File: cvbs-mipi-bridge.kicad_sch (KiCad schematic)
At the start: 107 parts, among them IC1 ADV7280BCPZ-M, IC2 TLV70018, IC4 SN74AUP1G17DCKR, IC5 SN74AUP1G17DCKR, J1 WE_68715014522, J2 1053131102, J3 KLPX-0848A-2-Y, J4 KLPX-0848A-2-Y, J5 KLPX-0848A-2-Y, J6 KLPX-0848A-2-Y, J7 61300211121, Q1 BSS138APW, Q2 BSS138APW, Q3 BSS138APW, Q4 BSS138APW, Y1 ABM8G-28.63636MHZ-18-D2Y-T

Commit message: Routing (WiP)
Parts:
- removed R30: R_0R_0402, cvbs-mipi-bridge-footprints:0402-res, symbol cvbs-mipi-bridge:R_0R_0402
- added R30: R_0R_0805, cvbs-mipi-bridge-footprints:0805-res, symbol cvbs-mipi-bridge:R_0R_0805
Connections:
- net 1V8_SYS: now also R30.2
- net at C9.1, IC2.5 (VOUT), TP3.1: now also R30.1
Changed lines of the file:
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@@
     (pin "4")
-  )
-  (symbol (lib_id "cvbs-mipi-bridge:R_0R_0402") (at 174.625 36.83 0) (unit 1)
-    (in_bom yes) (on_board yes) (fields_autoplaced)
-    (property "Reference" "R30" (id 0) (at 174.625 31.8861 0)
-      (effects (font (size 1.524 1.524)))
-    )
-    (property "Value" "R_0R_0402" (id 1) (at 174.625 40.64 0)
-      (effects (font (size 1.524 1.524)) hide)
-    )
-    (property "Footprint" "cvbs-mipi-bridge-footprints:0402-res" (id 2) (at 179.705 31.75 0)
-      (effects (font (size 1.524 1.524)) (justify left) hide)
-    )
-    (property "Datasheet" "" (id 3) (at 174.625 36.83 0)
-      (effects (font (size 1.27 1.27)) hide)
-    )
-    (property "Manufacturer" "PANASONIC" (id 4) (at 179.705 26.67 0)
-      (effects (font (size 1.524 1.524)) (justify left) hide)
-    )
-    (property "MPN" "ERJ2GE0R00X" (id 5) (at 179.705 29.21 0)
-      (effects (font (size 1.524 1.524)) (justify left) hide)
-    )
-    (property "Val" "0R" (id 6) (at 174.625 34.6512 0))
-    (pin "1")
-    (pin "2")
   )
   (symbol (lib_id "cvbs-mipi-bridge:BSS138APW") (at 127 262.255 270) (unit 1)
@@
       (effects (font (size 1.524 1.524)) (justify left) hide)
     )
+    (pin "1")
+    (pin "2")
+  )
+  (symbol (lib_id "cvbs-mipi-bridge:R_0R_0805") (at 174.625 36.83 0) (unit 1)
+    (in_bom yes) (on_board yes)
+    (property "Reference" "R30" (id 0) (at 174.625 34.29 0)
+      (effects (font (size 1.524 1.524)))
+    )
+    (property "Value" "R_0R_0805" (id 1) (at 174.625 40.64 0)
+      (effects (font (size 1.524 1.524)) hide)
+    )
+    (property "Footprint" "cvbs-mipi-bridge-footprints:0805-res" (id 2) (at 179.705 31.75 0)
+      (effects (font (size 1.524 1.524)) (justify left) hide)
+    )
+    (property "Datasheet" "" (id 3) (at 174.625 36.83 0)
+      (effects (font (size 1.27 1.27)) hide)
+    )
+    (property "Manufacturer" "VISHAY" (id 4) (at 179.705 26.67 0)
+      (effects (font (size 1.524 1.524)) (justify left) hide)
+    )
+    (property "MPN" "CRCW08050000Z0EA" (id 5) (at 179.705 29.21 0)
+      (effects (font (size 1.524 1.524)) (justify left) hide)
+    )
+    (property "Val" "0R" (id 6) (at 174.625 39.37 0))
     (pin "1")
     (pin "2")
@@
       (reference "R29") (unit 1) (value "R_100k_0402") (footprint "cvbs-mipi-bridge-footprints:0402-res")
     )
-    (path "/935a0ed4-8ab8-4466-9793-5326c0b86bd1"
-      (reference "R30") (unit 1) (value "R_0R_0402") (footprint "cvbs-mipi-bridge-footprints:0402-res")
+    (path "/a2042ad6-c037-4bf6-86fd-f7cc9c142ea2"
+      (reference "R30") (unit 1) (value "R_0R_0805") (footprint "cvbs-mipi-bridge-footprints:0805-res")
     )
     (path "/61c0936f-710e-41ac-8508-01af59b77b09"

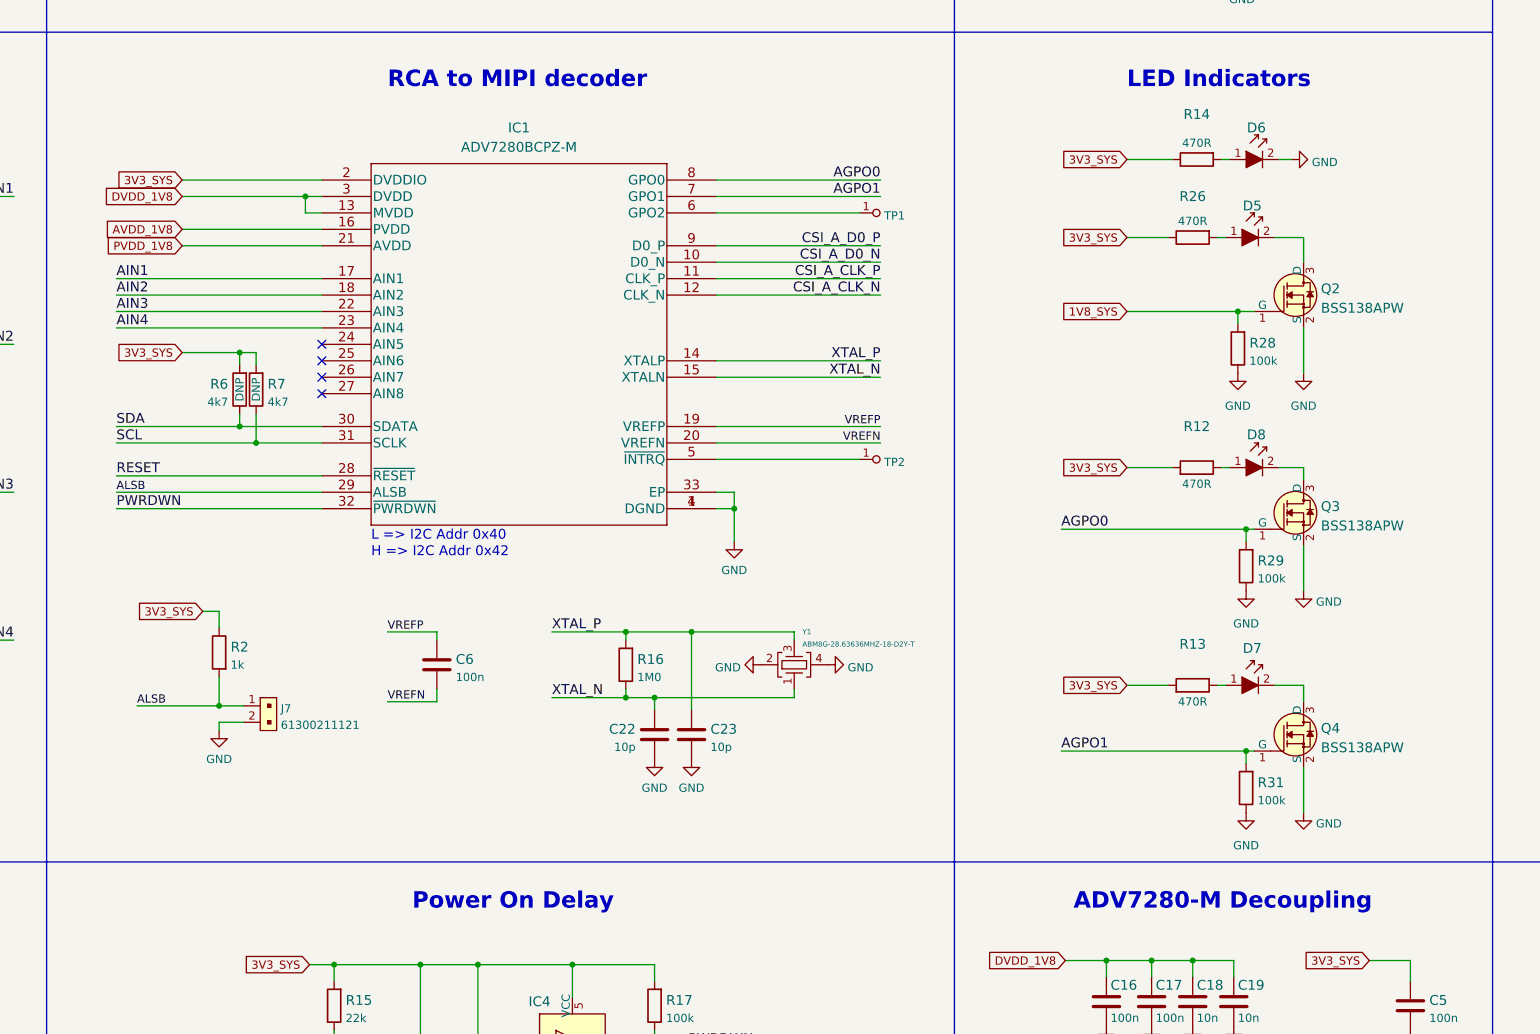
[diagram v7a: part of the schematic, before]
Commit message: Chip replaced with ADV7282-M
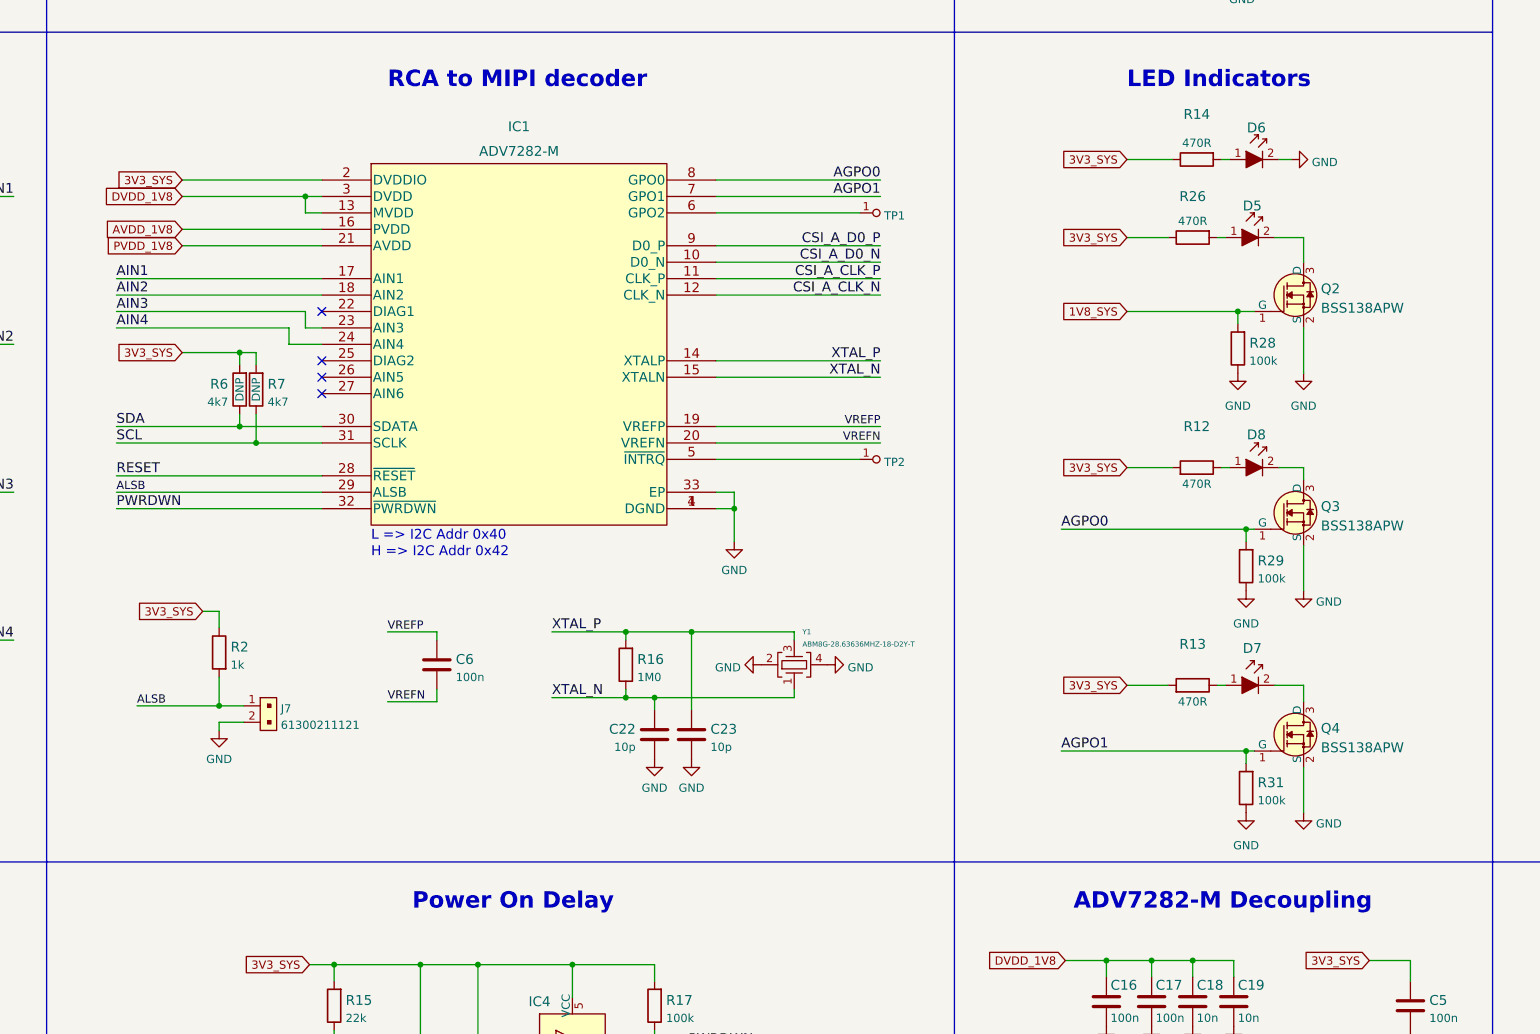
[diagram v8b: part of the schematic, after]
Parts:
- removed IC1: ADV7280BCPZ-M, cvbs-mipi-bridge-footprints:LFCSP-32-1EP-5x5mm, symbol cvbs-mipi-bridge:ADV7280BCPZ-M
- added IC1: ADV7282-M, antmicro-footprints:LFCSP-32-1EP-5x5mm, symbol antmicroDataAcquisitionAnalogtoDigitalConvertersADC:ADV7282-M
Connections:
- net 3V3_SYS: now also IC1.2 (DVDDIO)
- net AGPO0: now also IC1.8 (GPO0)
- net AGPO1: now also IC1.7 (GPO1)
- net AIN1: now also IC1.17 (AIN1)
- net AIN2: now also IC1.18 (AIN2)
- net AIN3: now also IC1.23 (AIN3)
- net AIN4: now also IC1.24 (AIN4)
- net ALSB: now also IC1.29 (ALSB)
- net AVDD_1V8: now also IC1.16 (PVDD)
- net CSI_A_CLK_N: now also IC1.12 (CLK_N)
- net CSI_A_CLK_P: now also IC1.11 (CLK_P)
- net CSI_A_D0_N: now also IC1.10 (D0_N)
- net CSI_A_D0_P: now also IC1.9 (D0_P)
- net DVDD_1V8: now also IC1.13 (MVDD), IC1.3 (DVDD)
- net GND: now also IC1.1 (DGND), IC1.33 (EP), IC1.4 (DGND)
- net PVDD_1V8: now also IC1.21 (AVDD)
- net PWRDWN: now also IC1.32 (~{PWRDWN})
- net RESET: now also IC1.28 (~{RESET})
- net SCL: now also IC1.31 (SCLK)
- net SDA: now also IC1.30 (SDATA)
- net VREFN: now also IC1.20 (VREFN)
- net VREFP: now also IC1.19 (VREFP)
- net XTAL_N: now also IC1.15 (XTALN)
- net XTAL_P: now also IC1.14 (XTALP)
- net at TP2.1: now also IC1.5 (~{INTRQ})
- net at TP1.1: now also IC1.6 (GPO2)
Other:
- note added: "ADV7282-M Decoupling"
- note removed: "ADV7280-M Decoupling"
- title: ModADV7280-M -> ModADV7282-M
